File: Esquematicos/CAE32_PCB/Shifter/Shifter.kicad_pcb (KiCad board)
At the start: 4 copper layers, 0 parts

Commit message: add: diseño de esquemático básico usando el microcontrolador rp2040
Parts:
- added J1: RJ45, Connector_RJ:RJ45_Amphenol_RJHSE538X, F.Cu at (155.6, 82.4)
- added J2: USB_C_Receptacle_USB2.0, Connector_USB:USB_C_Receptacle_G-Switch_GT-USB-7010ASV, F.Cu at (175.3, 78.7)
- added U1: RP2040, Package_DFN_QFN:QFN-56-1EP_7x7mm_P0.4mm_EP3.2x3.2mm, F.Cu at (170.1, 97.3)

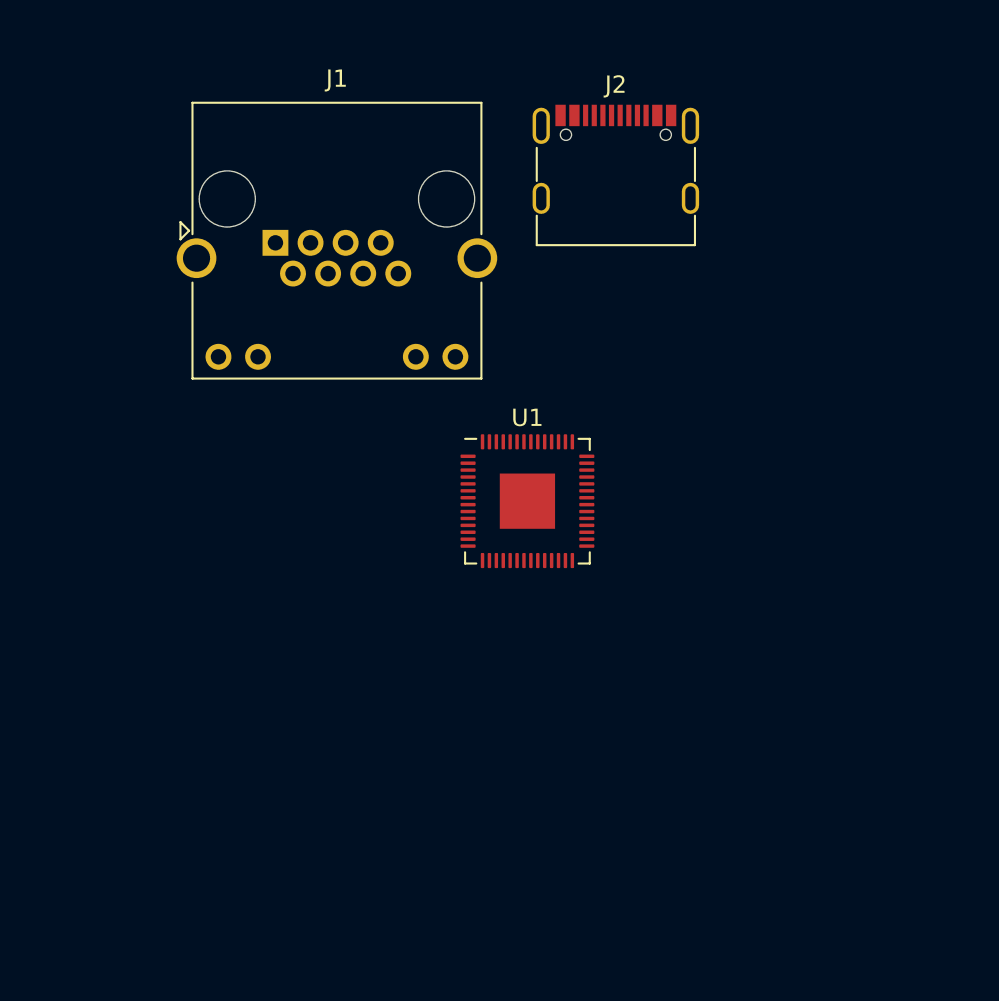
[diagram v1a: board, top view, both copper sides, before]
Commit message: update: se enruta completamente la pcb, aunque aun necesario un análisis posterior, ademas de agregar huellas e imagen de la pcb completa
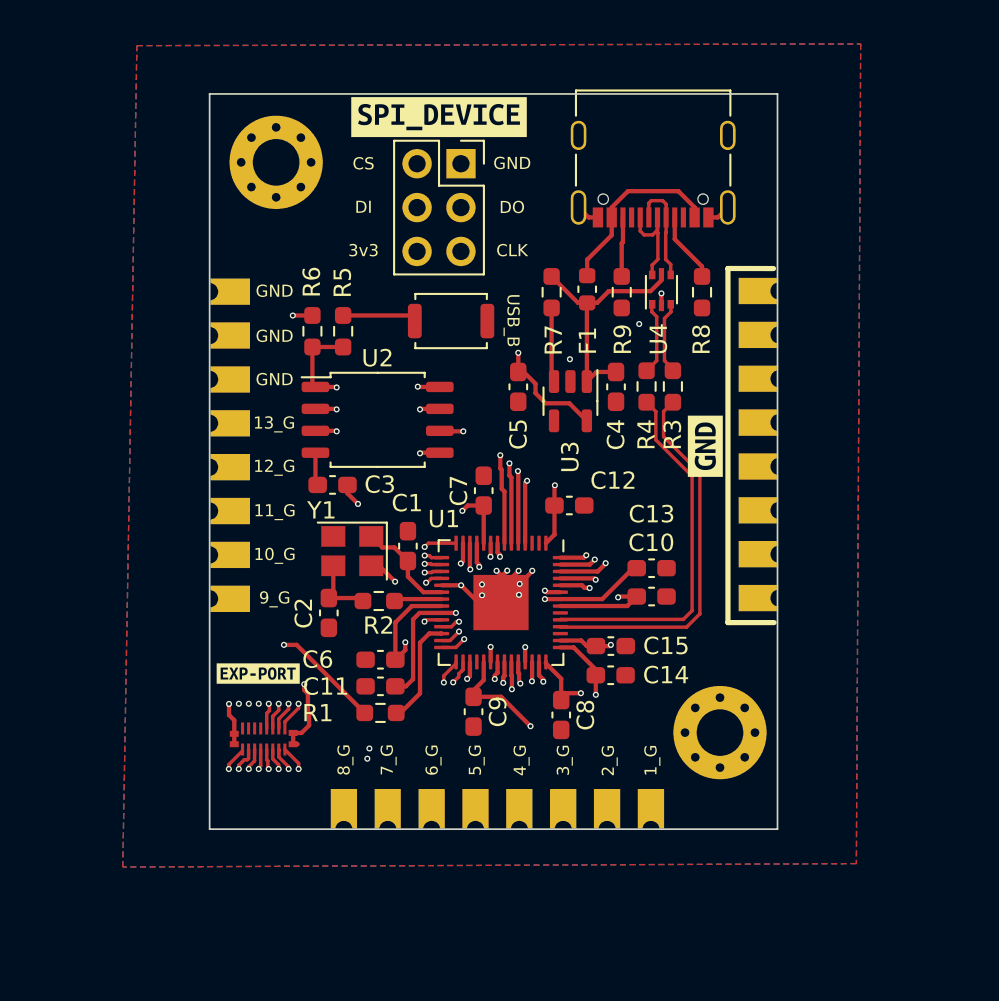
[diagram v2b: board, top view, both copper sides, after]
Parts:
- added C1: 22p, Capacitor_SMD:C_0603_1608Metric_Pad1.08x0.95mm_HandSolder, F.Cu at (163.2, 99.9)
- added C10: 0u1, Capacitor_SMD:C_0603_1608Metric_Pad1.08x0.95mm_HandSolder, F.Cu at (177.3, 102.8)
- added C11: 0u1, Capacitor_SMD:C_0603_1608Metric_Pad1.08x0.95mm_HandSolder, F.Cu at (161.6, 108.0)
- added C12: 0u1, Capacitor_SMD:C_0603_1608Metric_Pad1.08x0.95mm_HandSolder, F.Cu at (172.6, 97.6)
- added C13: 0u1, Capacitor_SMD:C_0603_1608Metric_Pad1.08x0.95mm_HandSolder, F.Cu at (177.3, 101.2)
- added C14: 0u1, Capacitor_SMD:C_0603_1608Metric_Pad1.08x0.95mm_HandSolder, F.Cu at (175.0, 107.4)
- added C15: 0u1, Capacitor_SMD:C_0603_1608Metric_Pad1.08x0.95mm_HandSolder, F.Cu at (175.0, 105.7)
- added C2: 22p, Capacitor_SMD:C_0603_1608Metric_Pad1.08x0.95mm_HandSolder, F.Cu at (158.6, 103.8)
- added C3: 0u1, Capacitor_SMD:C_0603_1608Metric_Pad1.08x0.95mm_HandSolder, F.Cu at (158.9, 96.4)
- added C4: 1u, Capacitor_SMD:C_0603_1608Metric_Pad1.08x0.95mm_HandSolder, F.Cu at (175.3, 90.7)
- added C5: 1u, Capacitor_SMD:C_0603_1608Metric_Pad1.08x0.95mm_HandSolder, F.Cu at (169.6, 90.7)
- added C6: 0u1, Capacitor_SMD:C_0603_1608Metric_Pad1.08x0.95mm_HandSolder, F.Cu at (161.6, 106.5)
- added C7: 0u1, Capacitor_SMD:C_0603_1608Metric_Pad1.08x0.95mm_HandSolder, F.Cu at (167.6, 96.7)
- added C8: 0u1, Capacitor_SMD:C_0603_1608Metric_Pad1.08x0.95mm_HandSolder, F.Cu at (172.1, 109.7)
- added C9: 0u1, Capacitor_SMD:C_0603_1608Metric_Pad1.08x0.95mm_HandSolder, F.Cu at (167.0, 109.5)
- added F1: 500mA, Fuse:Fuse_0603_1608Metric, F.Cu at (173.6, 85.0)
- added H1: MountingHole_Pad, MountingHole:MountingHole_2.7mm_M2.5_Pad_Via, F.Cu at (155.6, 77.7)
- added H2: MountingHole_Pad, MountingHole:MountingHole_2.7mm_M2.5_Pad_Via, F.Cu at (181.3, 110.7)
- added J3: Conn_01x08_Female, shifter:shi, F.Cu at (169.7, 116.3)
- added J4: Conn_01x08_Female, shifter:shi, F.Cu at (151.7, 95.3)
- added J5: Conn_01x08_Female, shifter:shi, F.Cu at (184.7, 92.8)
- added J6: USB_C_Receptacle_USB2.0, Connector_USB:USB_C_Receptacle_Palconn_UTC16-G, F.Cu at (177.4, 78.4)
- added R1: 1K, Resistor_SMD:R_0603_1608Metric_Pad0.98x0.95mm_HandSolder, F.Cu at (161.6, 109.6)
- added R2: 1k, Resistor_SMD:R_0603_1608Metric_Pad0.98x0.95mm_HandSolder, F.Cu at (161.5, 103.1)
- added R3: 27, Resistor_SMD:R_0603_1608Metric_Pad0.98x0.95mm_HandSolder, F.Cu at (178.6, 90.7)
- added R4: 27, Resistor_SMD:R_0603_1608Metric_Pad0.98x0.95mm_HandSolder, F.Cu at (177.0, 90.7)
- added R5: 1k, Resistor_SMD:R_0603_1608Metric_Pad0.98x0.95mm_HandSolder, F.Cu at (159.5, 87.5)
- added R6: 10k, Resistor_SMD:R_0603_1608Metric_Pad0.98x0.95mm_HandSolder, F.Cu at (157.7, 87.5)
- added R7: 10k, Resistor_SMD:R_0603_1608Metric_Pad0.98x0.95mm_HandSolder, F.Cu at (171.5, 85.2)
- added R8: 5k1, Resistor_SMD:R_0603_1608Metric_Pad0.98x0.95mm_HandSolder, F.Cu at (180.2, 85.2)
- added R9: 5k1, Resistor_SMD:R_0603_1608Metric_Pad0.98x0.95mm_HandSolder, F.Cu at (175.6, 85.2)
- added SW1: USB_BOOT, Button_Switch_SMD:SW_Push_SPST_NO_Alps_SKRK, F.Cu at (165.7, 86.9)
- added U2: W25Q16JVSNIQ, Package_SO:SOIC-8_5.23x5.23mm_P1.27mm, F.Cu at (161.5, 92.6)
- added U3: AP2112K-3.3, Package_TO_SOT_SMD:SOT-23-5, F.Cu at (172.6, 91.5)
- added U4: USBLC6-2P6, Package_TO_SOT_SMD:SOT-666, F.Cu at (177.9, 85.1)
- added Y1: 12Mhz, Crystal:Crystal_SMD_3225-4Pin_3.2x2.5mm, F.Cu at (160.0, 100.2)
- added kibuzzard-64B759C0: G***, kibuzzard-64B759C0, F.Cu at (165.0, 75.1)
- added kibuzzard-64B75A4D: G***, kibuzzard-64B75A4D, F.Cu at (180.4, 94.1)
- added kibuzzard-64B75D82: G***, kibuzzard-64B75D82, F.Cu at (154.6, 107.3)
- J1: value RJ45 -> Conn_01x18_Female; footprint Connector_RJ:RJ45_Amphenol_RJHSE538X -> shifter:BM28B0-6-16DS
- J2: value USB_C_Receptacle_USB2.0 -> SPI_DEVICE; footprint Connector_USB:USB_C_Receptacle_G-Switch_GT-USB-7010ASV -> Connector_PinSocket_2.54mm:PinSocket_2x03_P2.54mm_Vertical
- moved J1 28.7 mm to (154.9, 111.1), turned to 180 degrees
- moved J2 9.02 mm to (166.3, 77.8)
- moved U1 6.07 mm to (168.6, 103.2), turned to -90 degrees
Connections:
- net Net-(U1-Pad23) renamed /Power/1v1
- J1 pad 1: unconnected-(J1-Pad1) -> /GPIO_18
- J1 pad 10: (no net) -> unconnected-(J1-Pad10)
- J1 pad 11: (no net) -> unconnected-(J1-Pad11)
- J1 pad 12: (no net) -> unconnected-(J1-Pad12)
- J1 pad 2: unconnected-(J1-Pad2) -> /GPIO_17
- J1 pad 3: unconnected-(J1-Pad3) -> /GPIO_16
- J1 pad 4: unconnected-(J1-Pad4) -> /GPIO_15
- J1 pad 5: unconnected-(J1-Pad5) -> /GPIO_14
- J1 pad 6: unconnected-(J1-Pad6) -> /GPIO_13
- J1 pad 7: unconnected-(J1-Pad7) -> /GPIO_12
- J1 pad 8: unconnected-(J1-Pad8) -> /GPIO_11
- J1 pad 9: (no net) -> unconnected-(J1-Pad9)
- U1 pad 1: Net-(U1-Pad1) -> +3V3
- U1 pad 10: Net-(U1-Pad1) -> +3V3
- U1 pad 11: unconnected-(U1-Pad11) -> /11_GEAR
- U1 pad 12: unconnected-(U1-Pad12) -> /10_GEAR
- U1 pad 13: unconnected-(U1-Pad13) -> /9_GEAR
- U1 pad 14: unconnected-(U1-Pad14) -> /GPIO_11
- U1 pad 15: unconnected-(U1-Pad15) -> /GPIO_12
- U1 pad 16: unconnected-(U1-Pad16) -> /GPIO_13
- U1 pad 17: unconnected-(U1-Pad17) -> /GPIO_14
- U1 pad 18: unconnected-(U1-Pad18) -> /GPIO_15
- U1 pad 19: unconnected-(U1-Pad19) -> GNDREF
- U1 pad 20: unconnected-(U1-Pad20) -> /XIN
- U1 pad 21: unconnected-(U1-Pad21) -> /XOUT
- U1 pad 22: Net-(U1-Pad1) -> +3V3
- U1 pad 24: unconnected-(U1-Pad24) -> /SWCLK
- U1 pad 25: unconnected-(U1-Pad25) -> /SWDIO
- U1 pad 26: unconnected-(U1-Pad26) -> /RESET
- U1 pad 27: unconnected-(U1-Pad27) -> /GPIO_16
- U1 pad 28: unconnected-(U1-Pad28) -> /GPIO_17
- U1 pad 29: unconnected-(U1-Pad29) -> /GPIO_18
- U1 pad 30: unconnected-(U1-Pad30) -> /GPIO_19
- U1 pad 31: unconnected-(U1-Pad31) -> /GPIO_20
- U1 pad 33: Net-(U1-Pad1) -> +3V3
- U1 pad 34: unconnected-(U1-Pad34) -> /8_GEAR
- U1 pad 35: unconnected-(U1-Pad35) -> /7_GEAR
- U1 pad 36: unconnected-(U1-Pad36) -> /6_GEAR
- U1 pad 37: unconnected-(U1-Pad37) -> /5_GEAR
- U1 pad 38: unconnected-(U1-Pad38) -> /4_GEAR
- U1 pad 39: unconnected-(U1-Pad39) -> /3_GEAR
- U1 pad 4: unconnected-(U1-Pad4) -> /SPI_CLK
- U1 pad 40: unconnected-(U1-Pad40) -> /2_GEAR
- U1 pad 41: unconnected-(U1-Pad41) -> /1_GEAR
- U1 pad 42: Net-(U1-Pad1) -> +3V3
- U1 pad 43: unconnected-(U1-Pad43) -> +3V3
- U1 pad 44: unconnected-(U1-Pad44) -> +3V3
- U1 pad 46: unconnected-(U1-Pad46) -> /D-
- U1 pad 47: unconnected-(U1-Pad47) -> /D+
- U1 pad 49: Net-(U1-Pad1) -> +3V3
- U1 pad 5: unconnected-(U1-Pad5) -> /SPI_DO
- U1 pad 51: unconnected-(U1-Pad51) -> /QSPI_SD3
- U1 pad 52: unconnected-(U1-Pad52) -> /QSPI_SCK
- U1 pad 53: unconnected-(U1-Pad53) -> /QSPI_SD0
- U1 pad 54: unconnected-(U1-Pad54) -> /QSPI_SD2
- U1 pad 55: unconnected-(U1-Pad55) -> /QSPI_SD1
- U1 pad 56: unconnected-(U1-Pad56) -> /QSPI_CS
- U1 pad 57: unconnected-(U1-Pad57) -> GNDREF
- U1 pad 6: unconnected-(U1-Pad6) -> /SPI_DI
- U1 pad 7: unconnected-(U1-Pad7) -> /SPI_CS
- U1 pad 8: unconnected-(U1-Pad8) -> /13_GEAR
- U1 pad 9: unconnected-(U1-Pad9) -> /12_GEAR
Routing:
- net +3V3: track 0.00 -> 64.0 mm, vias 0 -> 14
- net /SPI_CS: track 0.00 -> 27.0 mm, vias 0 -> 1
- net /QSPI_CS: track 0.00 -> 25.5 mm, vias 0 -> 2
- net GNDREF: track 0.00 -> 24.1 mm, vias 0 -> 17
- net /SPI_DI: track 0.00 -> 23.7 mm, vias 0 -> 1
- net /QSPI_SD2: track 0.00 -> 23.5 mm, vias 0 -> 2
- net /GPIO_11: track 0.00 -> 22.9 mm, vias 0 -> 2
- net /QSPI_SD1: track 0.00 -> 22.2 mm, vias 0 -> 2
- net /SPI_DO: track 0.00 -> 21.9 mm, vias 0 -> 1
- net /D-: track 0.00 -> 21.8 mm
- net /GPIO_12: track 0.00 -> 21.4 mm, vias 0 -> 2
- net /13_GEAR: track 0.00 -> 21.0 mm, vias 0 -> 1
- net /D+: track 0.00 -> 21.0 mm
- net /9_GEAR: track 0.00 -> 20.8 mm, vias 0 -> 1
- net /GPIO_13: track 0.00 -> 20.3 mm, vias 0 -> 2
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- added copper zone on In1.Cu, net +3V3
- added copper zone on In2.Cu, net +3V3
- added copper zone on B.Cu, net GNDREF
- added copper zone on F.Cu, net GNDREF
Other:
- board outline added: 32.9 x 42.6 mm
- board text added: "10_G"
- board text added: "11_G"
- board text added: "12_G"
- board text added: "13_G"
- board text added: "1_G"
- board text added: "2_G"
- board text added: "3_G"
- board text added: "3v3"
- board text added: "4_G"
- board text added: "5_G"
- board text added: "6_G"
- board text added: "7_G"
- board text added: "8_G"
- board text added: "9_G"
- board text added: "CLK"
- board text added: "CS"
- board text added: "DI"
- board text added: "DO"
- board text added: "GND"
- board text added: "USB_B"

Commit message: update:Shifter PCB v1.1 Revision 1: Se cambia la posición de los "castelladed pins" a un solo lado, aumentando un poco el tamaño de la pcb pero reduciendo el costo de manufactura, ademas se añade la serigrafia correspondiente a la PCB
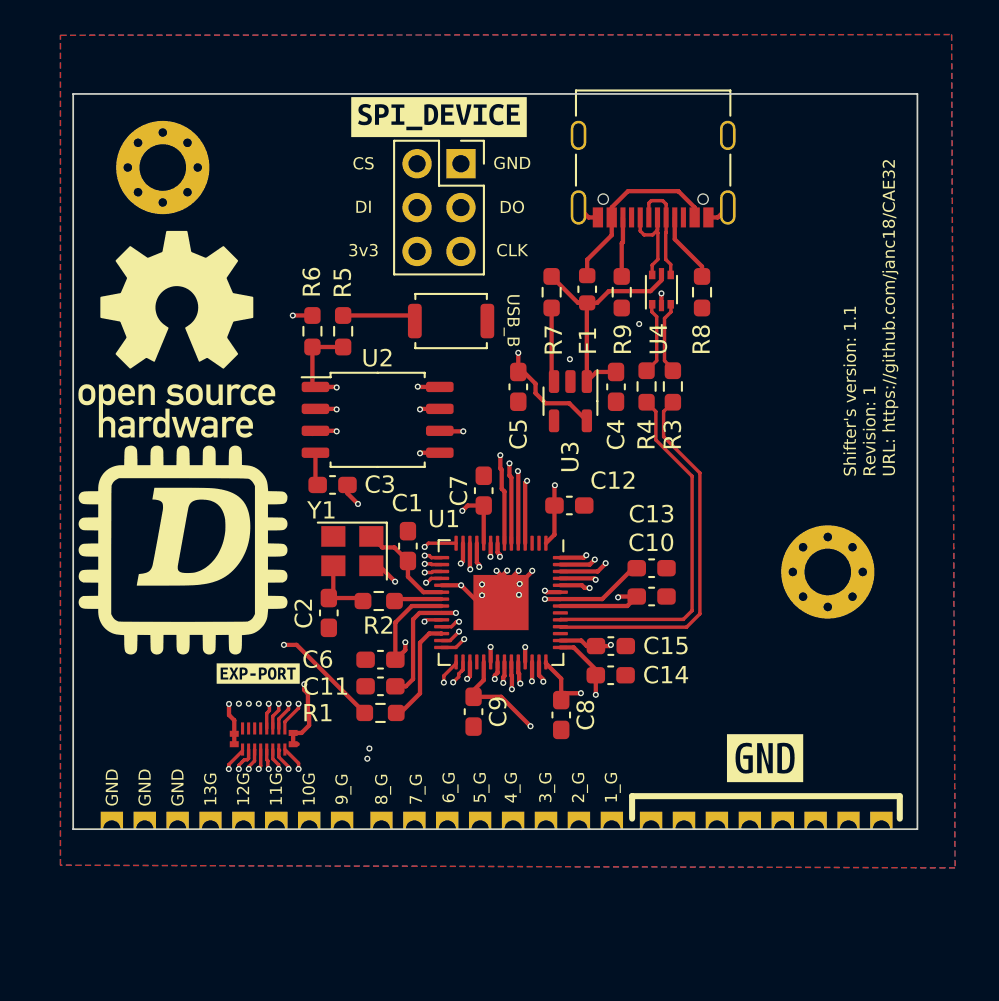
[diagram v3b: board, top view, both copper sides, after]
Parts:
- removed kibuzzard-64B75A4D: G***, kibuzzard-64B75A4D
- added kibuzzard-64F4C3CA: G***, kibuzzard-64F4C3CA, F.Cu at (183.9, 112.2)
- J1: value Conn_01x18_Female -> EXP-PORT
- R1: value 1K -> 1k
- moved J5 23.6 mm to (183.0, 116.3), turned to -90 degrees
- moved J4 21.0 mm to (151.8, 116.3), turned to -90 degrees
- moved H2 11.2 mm to (187.5, 101.4)
- moved H1 6.57 mm to (149.0, 78.0)
- moved J3 2.27 mm to (167.4, 116.3)
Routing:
- net /11_GEAR: track 20.1 -> 40.6 mm
- net /10_GEAR: track 20.2 -> 40.2 mm
- net /12_GEAR: track 19.2 -> 37.5 mm
- net /13_GEAR: track 21.0 -> 39.3 mm
- net /9_GEAR: track 20.8 -> 38.7 mm
- net /2_GEAR: track 13.7 -> 10.8 mm
- net /8_GEAR: track 17.0 -> 14.9 mm
- net /1_GEAR: track 13.5 -> 11.4 mm
- net /7_GEAR: track 13.7 -> 11.7 mm
- net /5_GEAR: track 12.2 -> 10.4 mm
- net GNDREF: track 24.1 -> 22.5 mm
- net /6_GEAR: track 13.0 -> 11.4 mm
- net /4_GEAR: track 9.87 -> 10.7 mm
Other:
- board size 32.9 x 42.6 mm -> 48.9 x 42.6 mm
- board text added: "10G"
- board text added: "11G"
- board text added: "12G"
- board text added: "13G"
- board text added: "Shifter's version: 1.1 Revision: 1 URL: https://github.com/janc18/CAE32"
- board text removed: "10_G"
- board text removed: "11_G"
- board text removed: "12_G"
- board text removed: "13_G"

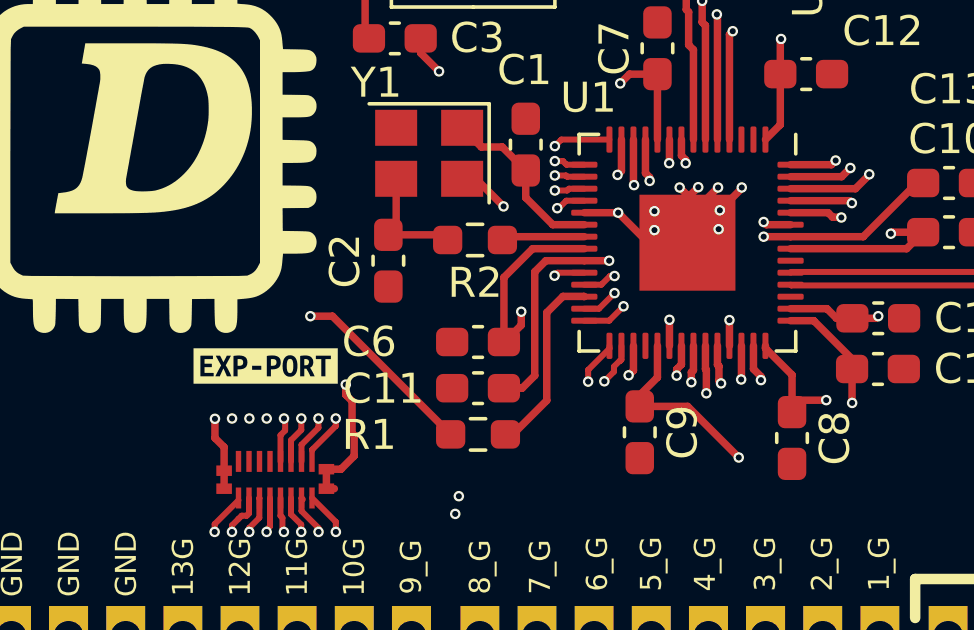
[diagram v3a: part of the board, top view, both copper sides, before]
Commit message: update: Se añade nombre y se separa a los diferentes componentes por categoria en el esquematico
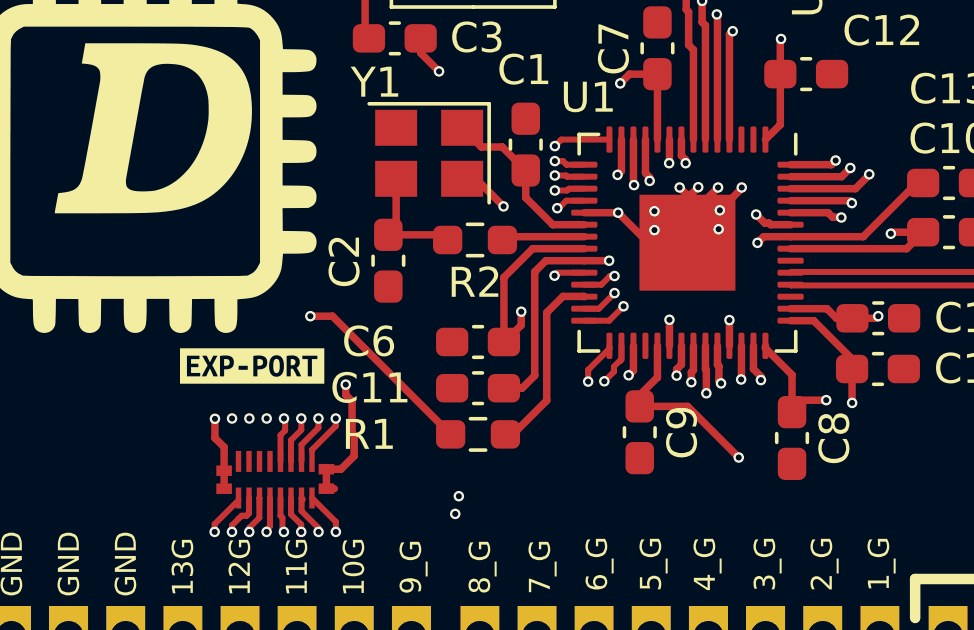
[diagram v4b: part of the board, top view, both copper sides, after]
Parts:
- H1, H2: value MountingHole_Pad -> MountingHole
- moved kibuzzard-64B75D82 0.45 mm to (154.1, 107.3)
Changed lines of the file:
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@@
     (attr board_only exclude_from_pos_files exclude_from_bom)
     (fp_text reference "kibuzzard-64F4C3CA" (at 0 -4.437063) (layer "F.SilkS") hide
-        (effects (font (size 0 0)))
+        (effects (font (size 0 0) (thickness 0.15)))
     )
     (fp_text value "G***" (at 0 4.437063) (layer "F.SilkS") hide
-        (effects (font (size 0 0)))
+        (effects (font (size 0 0) (thickness 0.15)))
     )
     (fp_poly
@@
   )
   (footprint "kibuzzard-64B75D82" (layer "F.Cu")
-    (at 154.55 107.3)
+    (at 154.1 107.3)
     (descr "Generated with KiBuzzard")
     (tags "kb_params=eyJBbGlnbm1lbnRDaG9pY2UiOiAiQ2VudGVyIiwgIkNhcExlZnRDaG9pY2UiOiAiWyIsICJDYXBSaWdodENob2ljZSI6ICJdIiwgIkZvbnRDb21ib0JveCI6ICJVYnVudHVNb25vLUIiLCAiSGVpZ2h0Q3RybCI6ICIwLjciLCAiTGF5ZXJDb21ib0JveCI6ICJGLlNpbGtTIiwgIk11bHRpTGluZVRleHQiOiAiRVhQLVBPUlQiLCAiUGFkZGluZ0JvdHRvbUN0cmwiOiAiNSIsICJQYWRkaW5nTGVmdEN0cmwiOiAiNSIsICJQYWRkaW5nUmlnaHRDdHJsIjogIjUiLCAiUGFkZGluZ1RvcEN0cmwiOiAiNSIsICJXaWR0aEN0cmwiOiAiIn0=")
@@
     (property "ki_keywords" "cap capacitor")
     (attr smd)
-    (fp_text reference "C11" (at 3.15 -0.02) (layer "F.SilkS")
+    (fp_text reference "C11" (at 3.58 -0.01) (layer "F.SilkS")
         (effects (font (size 1 1) (thickness 0.15)))
     )
@@
         (effects (font (size 1 1) (thickness 0.15)))
     )
-    (fp_text value "MountingHole_Pad" (at 0 3.7) (layer "F.Fab")
+    (fp_text value "MountingHole" (at 0 3.7) (layer "F.Fab")
         (effects (font (size 1 1) (thickness 0.15)))
     )
@@
         (effects (font (size 1 1) (thickness 0.15)))
     )
-    (fp_text value "MountingHole_Pad" (at 0 3.7) (layer "F.Fab")
+    (fp_text value "MountingHole" (at 0 3.7) (layer "F.Fab")
         (effects (font (size 1 1) (thickness 0.15)))
     )
@@
   (segment (start 162.4925 108.04) (end 163.1 108.04) (width 0.25) (layer "F.Cu") (net 26))
   (segment (start 176.26 101.2) (end 174.47 102.99) (width 0.25) (layer "F.Cu") (net 26))
+  (segment (start 172.0475 102.99) (end 171.15 102.99) (width 0.25) (layer "F.Cu") (net 26))
   (segment (start 163.1 108.04) (end 163.52 107.62) (width 0.25) (layer "F.Cu") (net 26))
   (segment (start 176.4675 101.2) (end 176.26 101.2) (width 0.25) (layer "F.Cu") (net 26))
@@
   (segment (start 163.52 104.16) (end 163.89 103.79) (width 0.25) (layer "F.Cu") (net 26))
   (segment (start 163.52 107.62) (end 163.52 104.16) (width 0.25) (layer "F.Cu") (net 26))
-  (segment (start 172.0475 102.99) (end 171.15 102.99) (width 0.25) (layer "F.Cu") (net 26))
+  (segment (start 171.15 102.99) (end 170.945 103.195) (width 0.25) (layer "F.Cu") (net 26))
   (segment (start 163.89 103.79) (end 165.1725 103.79) (width 0.25) (layer "F.Cu") (net 26))
   (via (at 166 103.79) (size 0.35) (drill 0.2) (layers "F.Cu" "B.Cu") (free) (net 26))
-  (via (at 171.15 102.99) (size 0.35) (drill 0.2) (layers "F.Cu" "B.Cu") (free) (net 26))
-  (segment (start 166 103.79) (end 170.35 103.79) (width 0.25) (layer "In1.Cu") (net 26))
-  (segment (start 170.35 103.79) (end 171.15 102.99) (width 0.25) (layer "In1.Cu") (net 26))
+  (via (at 170.945 103.195) (size 0.35) (drill 0.2) (layers "F.Cu" "B.Cu") (free) (net 26))
+  (segment (start 170.35 103.79) (end 166 103.79) (width 0.25) (layer "In1.Cu") (net 26))
+  (segment (start 170.945 103.195) (end 170.35 103.79) (width 0.25) (layer "In1.Cu") (net 26))
   (segment (start 162.5525 102.99) (end 165.1725 102.99) (width 0.25) (layer "F.Cu") (net 27))
   (segment (start 162.4425 103.1) (end 162.5525 102.99) (width 0.25) (layer "F.Cu") (net 27))
@@
   (segment (start 175.67 82.32) (end 175.67 80.89) (width 0.25) (layer "F.Cu") (net 39))
   (segment (start 165.066 91.9745) (end 163.952 91.9745) (width 0.25) (layer "F.Cu") (net 40))
-  (segment (start 171.24 102.59) (end 172.0475 102.59) (width 0.25) (layer "F.Cu") (net 40))
+  (segment (start 171.19 102.54) (end 171.336397 102.54) (width 0.25) (layer "F.Cu") (net 40))
+  (segment (start 170.9 102.25) (end 171.19 102.54) (width 0.25) (layer "F.Cu") (net 40))
   (segment (start 163.952 91.9745) (end 163.92 92.0065) (width 0.25) (layer "F.Cu") (net 40))
-  (segment (start 171.15 102.5) (end 171.24 102.59) (width 0.25) (layer "F.Cu") (net 40))
+  (segment (start 171.386397 102.59) (end 172.0475 102.59) (width 0.25) (layer "F.Cu") (net 40))
+  (segment (start 171.336397 102.54) (end 171.386397 102.59) (width 0.25) (layer "F.Cu") (net 40))
   (via (at 163.92 92.0065) (size 0.35) (drill 0.2) (layers "F.Cu" "B.Cu") (net 40))
-  (via (at 171.15 102.5) (size 0.35) (drill 0.2) (layers "F.Cu" "B.Cu") (net 40))
-  (segment (start 171.15 102.5) (end 171.15 99.56) (width 0.25) (layer "In1.Cu") (net 40))
+  (via (at 170.9 102.25) (size 0.35) (drill 0.2) (layers "F.Cu" "B.Cu") (net 40))
+  (segment (start 167.67 96.08) (end 164.53 96.08) (width 0.25) (layer "In1.Cu") (net 40))
   (segment (start 164.53 96.08) (end 162.48 94.03) (width 0.25) (layer "In1.Cu") (net 40))
-  (segment (start 162.48 93.4465) (end 163.92 92.0065) (width 0.25) (layer "In1.Cu") (net 40))
   (segment (start 162.48 94.03) (end 162.48 93.4465) (width 0.25) (layer "In1.Cu") (net 40))
-  (segment (start 167.67 96.08) (end 164.53 96.08) (width 0.25) (layer "In1.Cu") (net 40))
-  (segment (start 171.15 99.56) (end 167.67 96.08) (width 0.25) (layer "In1.Cu") (net 40))
+  (segment (start 170.9 102.25) (end 170.9 99.31) (width 0.25) (layer "In1.Cu") (net 40))
+  (segment (start 162.48 93.4465) (end 163.92 92.0065) (width 0.25) (layer "In1.Cu") (net 40))
+  (segment (start 170.9 99.31) (end 167.67 96.08) (width 0.25) (layer "In1.Cu") (net 40))
   (segment (start 172.0475 102.19) (end 173.3 102.19) (width 0.25) (layer "F.Cu") (net 41))
   (segment (start 165.098 93.2765) (end 165.066 93.2445) (width 0.25) (layer "F.Cu") (net 41))
